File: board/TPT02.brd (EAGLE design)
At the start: 28 x 28 mm, 20 parts, among them SW4 SW_SLIDECUS12, U1 MOD_CYBLE022001-00, U2 REG_LTC1502

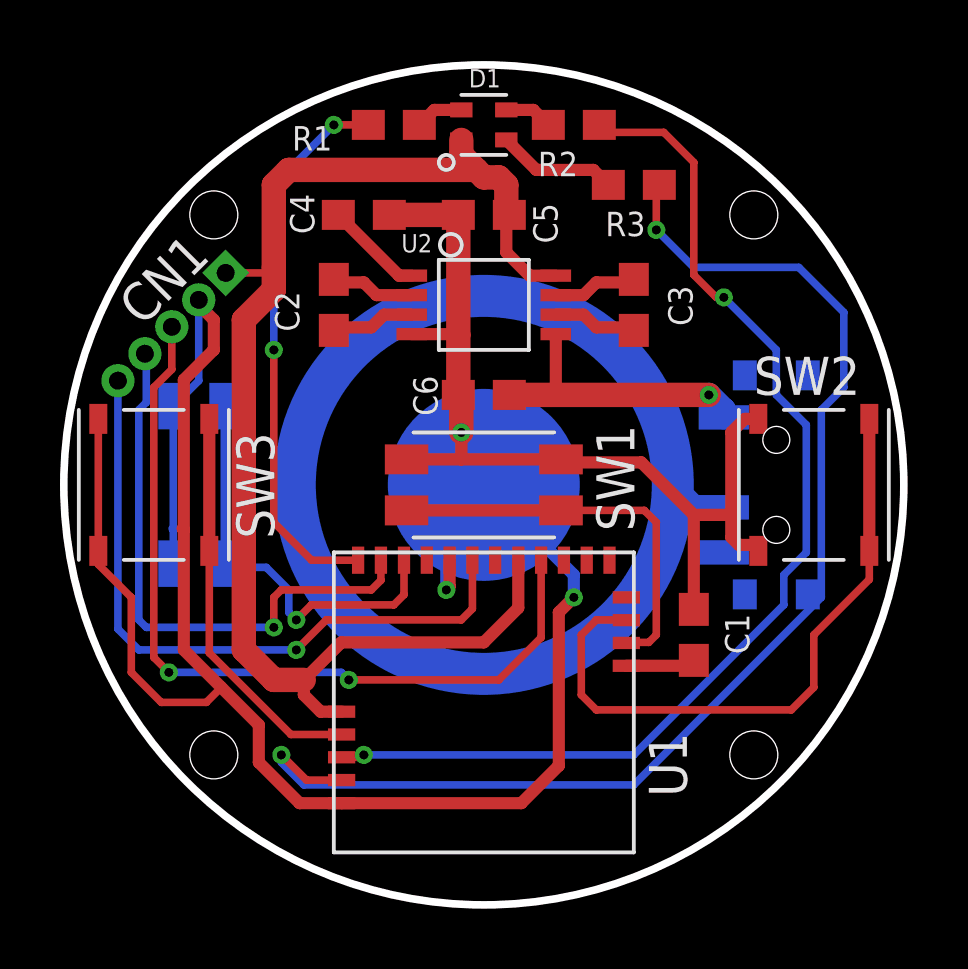
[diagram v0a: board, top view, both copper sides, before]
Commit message: 基板の修正（バッテリ電圧計測＆TXD端子）
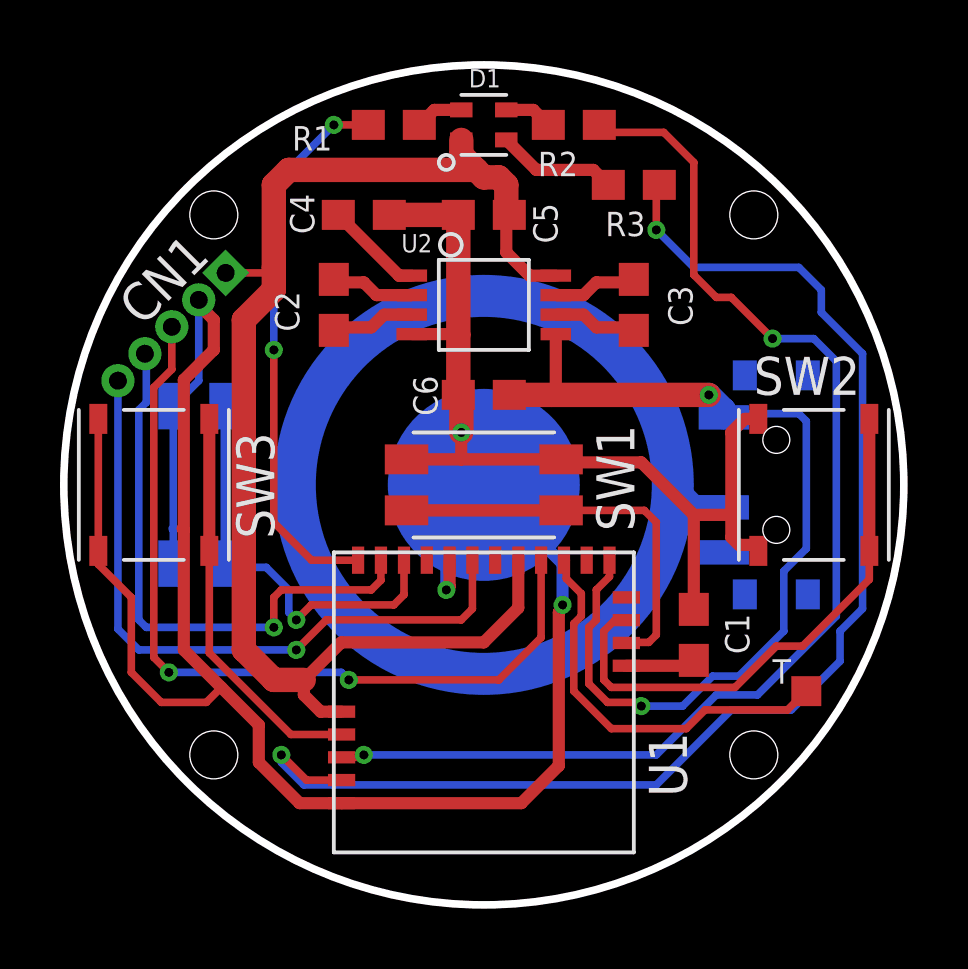
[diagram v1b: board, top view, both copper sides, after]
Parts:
- added CNM1: CON_P01SMD1MM, akita:PAD_SMD1MM
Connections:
- new net TXD: CNM1.P$1, U1.P$15
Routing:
- net VBAT: track 9.69 -> 32.2 mm, vias 1 -> 2
- net TXD: track 0.00 -> 13.6 mm
- net SWB: track 21.7 -> 18.3 mm
- net LED_A: track 37.3 -> 40.5 mm
- net LED_C: track 42.2 -> 44.4 mm
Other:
- board text added: "T"
- board text added: "t=0.6mm"

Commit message: 両脇のスイッチ(SWB/SWO)のパッケージを変更
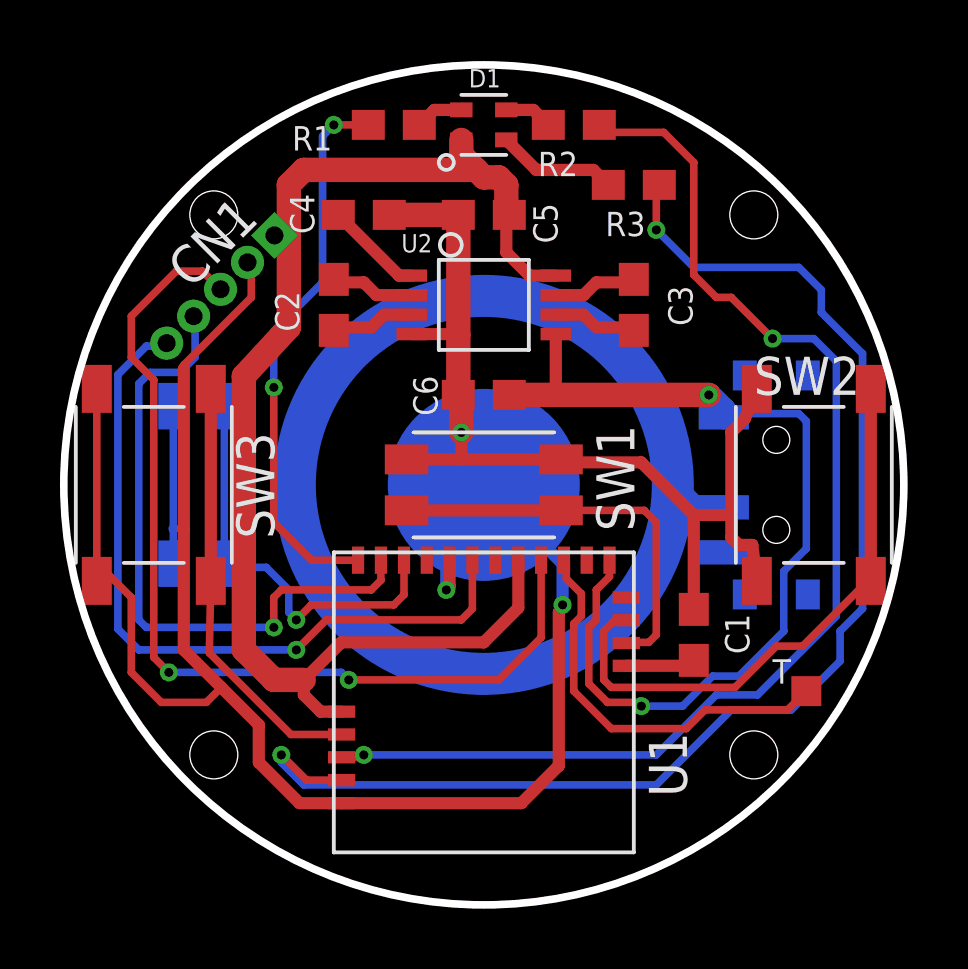
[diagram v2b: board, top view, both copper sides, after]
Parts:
- SW2, SW3: device akita:SW_TSKA-2JL -> akita:SW_PTS525SK08
- moved CN1 2.05 mm to (5.22, 20.5)
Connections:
- net GND: now also SW2.P$B1, SW2.P$B2, SW3.P$B1, SW3.P$B2; no longer SW2.PB1, SW2.PB2, SW3.PB1, SW3.PB2
- net SWB: now also SW2.P$A1, SW2.P$A2; no longer SW2.PA1, SW2.PA2
- net SWO: now also SW3.P$A1, SW3.P$A2; no longer SW3.PA1, SW3.PA2
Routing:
- net XRES: track 27.7 -> 31.9 mm
- net P07: track 19.1 -> 21.6 mm
- net P06: track 22.6 -> 24.8 mm
- net GND: track 100.0 -> 101.4 mm
- net +3V3: track 45.4 -> 44.1 mm
- net SWB: track 18.3 -> 19.4 mm
- net SWO: track 13.3 -> 14.3 mm
